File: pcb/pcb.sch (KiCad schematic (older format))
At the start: 9 parts, among them J1 Conn_01x02, J2 Conn_01x04_Male, U1 MCP73811T-420I-OT, U2 LD39050PU33R, U3 ESP8266-12E_ESP-12E

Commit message: finish the shcematic design
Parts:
- removed D1: D_Schottky, Diode_SMD:D_SMA_Handsoldering, symbol Device:D_Schottky
- removed J2: Conn_01x04_Male, Connector_PinSocket_2.54mm:PinSocket_1x04_P2.54mm_Vertical, symbol Connector:Conn_01x04_Male
- removed RN?: R_Pack04, symbol Device:R_Pack04
- removed U1: MCP73811T-420I-OT, Package_TO_SOT_SMD:SOT-23-5, symbol Battery_Management:MCP73811T-420I-OT
- removed U2: LD39050PU33R, SON95P300X300X100-7N, symbol LD39050PU33R:LD39050PU33R
- removed U3: ESP8266-12E_ESP-12E, XCVR_ESP8266-12E/ESP-12E, symbol ESP8266-12E_ESP-12E:ESP8266-12E_ESP-12E
- added C3: 10u, Capacitor_SMD:C_0603_1608Metric_Pad1.05x0.95mm_HandSolder, symbol Device:C
- added C4: 100nF, Capacitor_SMD:C_0603_1608Metric, symbol Device:C
- added C5, C6, C7: 100n, Capacitor_SMD:C_0603_1608Metric, symbol Device:C
- added D1: SP0503BAHTG, digikey-footprints:SOT-143-4, symbol dk_TVS-Diodes:SP0503BAHTG
- added H1, H2, H3: MountingHole_Pad, MountingHole:MountingHole_3.2mm_M3_DIN965_Pad, symbol Mechanical:MountingHole_Pad
- added H4: MountingHole_Pad, MountingHole:MountingHole_3.2mm_M3, symbol Mechanical:MountingHole_Pad
- added J2: USB_B_Micro, Connector_USB:USB_Micro-B_Molex-105017-0001, symbol Connector:USB_B_Micro
- added Q1: Si2371EDS, Package_TO_SOT_SMD:SOT-23, symbol Transistor_FET:Si2371EDS
- added Q2, Q3: MMBT2222A-TP, digikey-footprints:SOT-23-3, symbol dk_Transistors-Bipolar-BJT-Single:MMBT2222A-TP
- added R1: 2k, Resistor_SMD:R_0603_1608Metric_Pad1.05x0.95mm_HandSolder, symbol Device:R_US
- added R10, R11, R12, R9: 10k, Resistor_SMD:R_0603_1608Metric, symbol Device:R_US
- added R2, R3: 10k, Resistor_SMD:R_0603_1608Metric_Pad1.05x0.95mm_HandSolder, symbol Device:R_US
- added R4: R_Pack04_Split, Resistor_SMD:R_Array_Concave_4x0603, symbol Device:R_Pack04_Split
- added R5, R6: 100k, Resistor_SMD:R_0603_1608Metric_Pad1.05x0.95mm_HandSolder, symbol Device:R_US
- added R7, R8: 10k, Resistor_SMD:R_Array_Concave_4x0603, symbol Device:R_Pack04_Split
- added U1: LD1117S33CTR, digikey-footprints:SOT-223, symbol dk_PMIC-Voltage-Regulators-Linear:LD1117S33CTR
- added U2: MCP73831-2-OT, Package_TO_SOT_SMD:SOT-23-5, symbol Battery_Management:MCP73831-2-OT
- added U3: CP2104, Package_DFN_QFN:QFN-24-1EP_4x4mm_P0.5mm_EP2.6x2.6mm, symbol Interface_USB:CP2104
- added U4: CCS811, Package_LGA:AMS_LGA-10-1EP_2.7x4mm_P0.6mm, symbol Sensor_Gas:CCS811
- added U5: ESP-12F, RF_Module:ESP-12E, symbol RF_Module:ESP-12F
- added U6: BME280, digikey-footprints:Pressure_Sensor_LGA-8_2.5x2.5mm_BME280, symbol dk_Humidity-Moisture-Sensors:BME280
- added U7: TSL2561, Kevin_Lutzer:TSL2561, symbol Kevin_Lutzer:TSL2561
- C1: value 1uf -> 1u
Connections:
- net labels added: BAT_LVL, CCS_nINT, I2C_SCK, I2C_SDA, UART_RX, UART_TX, nBAT_STAT, nBOOT, nINT, nRST
- net labels removed: BOOT, EN, RST, RX, TX
- wire segments 47 -> 163
- no-connect marks 0 -> 26
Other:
- note added: "1K - 1A\n2K - 500mA\n10K - 100mA\n"
- note added: "Lipo Charger and Regulator"
- note added: "Sensor Array"
- note added: "The CP210x series of chips requires a driver. There is also a built in Boot/Rst trigger using the DTR and RTS controls.\nhttps://www.silabs.com/products/development-tools/software/usb-to-uart-bridge-vcp-drivers"
- note added: "USB Bridge"
- moved on the sheet: C1, C2

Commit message: get the update done on the pcb design, finish it
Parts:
- removed R10, R11, R12, R9: 10k, Resistor_SMD:R_0603_1608Metric, symbol Device:R_US
- removed R2, R3: 10k, Resistor_SMD:R_0603_1608Metric_Pad1.05x0.95mm_HandSolder, symbol Device:R_US
- removed unit 4 of R4
- removed unit 3 of R4
- removed U1: LD1117S33CTR, digikey-footprints:SOT-223, symbol dk_PMIC-Voltage-Regulators-Linear:LD1117S33CTR
- added D2: MBR120ESFT1G, Diode_SMD:D_SOD-123, symbol Kevin_Lutzer:MBR120ESFT1G
- added R2: 10k, Resistor_SMD:R_Array_Convex_4x0603, symbol Device:R_Pack04_Split
- added R9: 10k, Resistor_SMD:R_Array_Convex_4x1206, symbol Device:R_Pack04_Split
- added SW1: PCM12, Button_Switch_SMD:SW_SPDT_PCM12, symbol Switch:SW_SPDT
- added U1: LD56100, Package_DFN_QFN:DFN-8-1EP_2x2mm_P0.45mm_EP0.64x1.38mm, symbol Kevin_Lutzer:LD56100
- H1, H2, H3: footprint MountingHole:MountingHole_3.2mm_M3_DIN965_Pad -> MountingHole:MountingHole_2.2mm_M2_DIN965_Pad
- H4: footprint MountingHole:MountingHole_3.2mm_M3 -> MountingHole:MountingHole_2.2mm_M2
- R4: value R_Pack04_Split -> 10k
- R7: footprint Resistor_SMD:R_Array_Concave_4x0603 -> Resistor_SMD:R_Array_Convex_4x1206
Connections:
- net labels added: CCS_nWAKE
- wire segments 163 -> 184
- no-connect marks 26 -> 25
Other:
- moved on the sheet: C1, C2, H1, H2, H3, H4, R5, R6, R7A, R7B, R8A, R8B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

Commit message: try update the node modules
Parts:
- removed C1: 1u, Capacitor_SMD:C_0603_1608Metric_Pad1.05x0.95mm_HandSolder, symbol Device:C
- removed C5, C6, C7: 100n, Capacitor_SMD:C_0603_1608Metric, symbol Device:C
- removed D1: SP0503BAHTG, digikey-footprints:SOT-143-4, symbol dk_TVS-Diodes:SP0503BAHTG
- removed D2: MBR120ESFT1G, Diode_SMD:D_SOD-123, symbol Kevin_Lutzer:MBR120ESFT1G
- removed H2, H3: MountingHole_Pad, MountingHole:MountingHole_2.2mm_M2_DIN965_Pad, symbol Mechanical:MountingHole_Pad
- removed J1: Conn_01x02, Connector_JST:JST_XH_S2B-XH-A-1_1x02_P2.50mm_Horizontal, symbol Connector_Generic:Conn_01x02
- removed J2: USB_B_Micro, Connector_USB:USB_Micro-B_Molex-105017-0001, symbol Connector:USB_B_Micro
- removed Q1: Si2371EDS, Package_TO_SOT_SMD:SOT-23, symbol Transistor_FET:Si2371EDS
- removed Q2, Q3: MMBT2222A-TP, digikey-footprints:SOT-23-3, symbol dk_Transistors-Bipolar-BJT-Single:MMBT2222A-TP
- removed R1: 2k, Resistor_SMD:R_0603_1608Metric_Pad1.05x0.95mm_HandSolder, symbol Device:R_US
- removed R2: 10k, Resistor_SMD:R_Array_Convex_4x0603, symbol Device:R_Pack04_Split
- removed R4, R8: 10k, Resistor_SMD:R_Array_Concave_4x0603, symbol Device:R_Pack04_Split
- removed R5, R6: 100k, Resistor_SMD:R_0603_1608Metric_Pad1.05x0.95mm_HandSolder, symbol Device:R_US
- removed R7, R9: 10k, Resistor_SMD:R_Array_Convex_4x1206, symbol Device:R_Pack04_Split
- removed U2: MCP73831-2-OT, Package_TO_SOT_SMD:SOT-23-5, symbol Battery_Management:MCP73831-2-OT
- removed U4: CCS811, Package_LGA:AMS_LGA-10-1EP_2.7x4mm_P0.6mm, symbol Sensor_Gas:CCS811
- removed U7: TSL2561, Kevin_Lutzer:TSL2561, symbol Kevin_Lutzer:TSL2561
- added C10: 1u, Capacitor_SMD:C_0603_1608Metric, symbol Device:C
- added C8: 10u, Capacitor_SMD:C_0603_1608Metric, symbol Device:C
- added C9, C? (x3): 100n, Capacitor_SMD:C_0603_1608Metric, symbol Device:C
- added D1: WS2812B, LED_SMD:LED_WS2812B_PLCC4_5.0x5.0mm_P3.2mm, symbol LED:WS2812B
- added H? (x2): MountingHole_Pad, MountingHole:MountingHole_2.2mm_M2_ISO14580_Pad, symbol Mechanical:MountingHole_Pad
- added J1: USB_B_Mini, Connector_USB:USB_Micro-B_Molex-105017-0001, symbol Connector:USB_B_Mini
- added Q1, Q2: BSS138DW-7-F, digikey-footprints:SOT-363, symbol dk_Transistors-FETs-MOSFETs-Arrays:BSS138DW-7-F
- added R2, R3, R4: 10k, Resistor_SMD:R_0603_1608Metric, symbol Device:R_US
- added R5, RN1: 10k, Resistor_SMD:R_Array_Convex_4x0603, symbol Device:R_Pack04_Split
- added SW2, SW3: PTS645Vx83, Button_Switch_THT:SW_Tactile_SPST_Angled_PTS645Vx58-2LFS, symbol Switch:SW_SPST
- added U2: MIC5225-1.8YM5, Package_TO_SOT_SMD:SOT-23-5, symbol Regulator_Linear:MIC5504-1.8YM5
- added U4: TSL2591, Kevin_Lutzer:TSL2591, symbol Kevin_Lutzer:TSL2591
- added U7: SGP30, Kevin_Lutzer:SGP30, symbol Kevin_Lutzer:SGP30
- added U?: LD1117S33CTR, digikey-footprints:SOT-223, symbol dk_PMIC-Voltage-Regulators-Linear:LD1117S33CTR
- C2: footprint Capacitor_SMD:C_0603_1608Metric_Pad1.05x0.95mm_HandSolder -> Capacitor_SMD:C_0805_2012Metric
- C3: value 10u -> 100n; footprint Capacitor_SMD:C_0603_1608Metric_Pad1.05x0.95mm_HandSolder -> Capacitor_SMD:C_0603_1608Metric
- C4: value 100nF -> 1u
- H1: footprint MountingHole:MountingHole_2.2mm_M2_DIN965_Pad -> MountingHole:MountingHole_2.2mm_M2
- SW1: value PCM12 -> OS102011MA1QN1‎; footprint Button_Switch_SMD:SW_SPDT_PCM12 -> Button_Switch_THT:SW_CuK_OS102011MA1QN1_SPDT_Angled
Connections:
- net labels added: +1V8, MODE, RGB_LED, UART_DTR, UART_RTS
- net labels removed: +BATT, BAT_LVL, CCS_nINT, CCS_nWAKE, nBAT_STAT
- wire segments 184 -> 180
- no-connect marks 25 -> 28
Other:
- note added: "Regulators (3.3V and 1.8V)"
- note added: "The 3.3V Regulator is rated at 1A, It is to supply power to the ESP and most\nof the sensors. The 1.8V Regular is rated at 150mA and is for the CP60 gas\nsensor."
- note added: "Trigger circuit for the boot/rst \nesp8266 sequence needed for \nprogramming"
- note removed: "1K - 1A\n2K - 500mA\n10K - 100mA\n"
- note removed: "Lipo Charger and Regulator"
- moved on the sheet: C2, C4, H4, U6

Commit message: update the pcb stuff
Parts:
- removed Q2: BSS138DW-7-F, digikey-footprints:SOT-363, symbol dk_Transistors-FETs-MOSFETs-Arrays:BSS138DW-7-F
- removed RN1: 10k, Resistor_SMD:R_Array_Convex_4x0603, symbol Device:R_Pack04_Split
- removed SW1: OS102011MA1QN1‎, Button_Switch_THT:SW_CuK_OS102011MA1QN1_SPDT_Angled, symbol Switch:SW_SPDT
- removed U1: LD56100, Package_DFN_QFN:DFN-8-1EP_2x2mm_P0.45mm_EP0.64x1.38mm, symbol Kevin_Lutzer:LD56100
- removed U4: TSL2591, Kevin_Lutzer:TSL2591, symbol Kevin_Lutzer:TSL2591
- removed U6: BME280, digikey-footprints:Pressure_Sensor_LGA-8_2.5x2.5mm_BME280, symbol dk_Humidity-Moisture-Sensors:BME280
- removed U7: SGP30, Kevin_Lutzer:SGP30, symbol Kevin_Lutzer:SGP30
- removed U?: LD1117S33CTR, digikey-footprints:SOT-223, symbol dk_PMIC-Voltage-Regulators-Linear:LD1117S33CTR
- added D2: SP0503BAHT, Package_TO_SOT_SMD:SOT-143, symbol Power_Protection:SP0503BAHT
- added SW1: PTS645Vx83, Button_Switch_THT:SW_Tactile_SPST_Angled_PTS645Vx58-2LFS, symbol Switch:SW_SPST
- added U1: AP2112K-3.3, Package_TO_SOT_SMD:SOT-23-5, symbol Regulator_Linear:AP2112K-3.3
- C2: value 10u -> 47u
- C4: value 1u -> 100n
- C8: footprint Capacitor_SMD:C_0603_1608Metric -> Capacitor_SMD:C_0805_2012Metric
- Q1: symbol dk_Transistors-FETs-MOSFETs-Arrays:BSS138DW-7-F -> pcb-rescue:BSS138DW-7-F-dk_Transistors-FETs-MOSFETs-Arrays
- gave numbers to parts that had none: 5
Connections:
- net labels removed: UART_DTR, UART_RTS
- wire segments 180 -> 140
- no-connect marks 28 -> 26
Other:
- note added: "I/O - Buttons and LEDs"
- note added: "USB/UART Bridge + Auto Reset"
- note removed: "Sensor Array"
- note removed: "USB Bridge"
- moved on the sheet: C1, C10, C2, C3, C5, C6, C8, C9, D1, H1, H2, H3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

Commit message: finish laying out most of the pcb parts
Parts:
- removed C3: 100n, Capacitor_SMD:C_0603_1608Metric, symbol Device:C
- removed Q1: BSS138DW-7-F, digikey-footprints:SOT-363, symbol pcb-rescue:BSS138DW-7-F-dk_Transistors-FETs-MOSFETs-Arrays
- removed R5: 10k, Resistor_SMD:R_Array_Convex_4x0603, symbol Device:R_Pack04_Split
- added C7: 10u, Capacitor_SMD:C_0805_2012Metric, symbol Device:C
- added D3, D4: LED, LED_SMD:LED_0603_1608Metric, symbol Device:LED
- added Q1: BSS138DW-7-F, digikey-footprints:SOT-363, symbol dk_Transistors-FETs-MOSFETs-Arrays:BSS138DW-7-F
- added R1, R6: 470, Resistor_SMD:R_0603_1608Metric, symbol Device:R_Small_US
- added R5, R7, R8, R9: 10k, Resistor_SMD:R_0603_1608Metric, symbol Device:R_Small_US
- C10: value 1u -> 10u
- C9: value 100n -> 10u
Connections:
- net +3V3: now also C1.1, D3.1 (K), D4.1 (K), R5.1, R7.1, R8.1; no longer C9.1, U2.1 (VIN), U2.3 (EN)
- net +5V: now also C9.1, D2.2 (K), U2.1 (VIN), U2.3 (EN), C7.1; no longer D2.4 (K)
- net GND: now also C7.2, R9.2
- net MODE: now also SW1.2 (B), U5.7 (GPIO13); no longer SW3.2 (B), U5.14 (SCLK)
- net nBOOT: now also SW2.2 (B), Q1.3 (D1), R8.2; no longer SW1.2 (B)
- net nRST: now also SW3.2 (B), Q1.6 (D2), R5.2; no longer C1.1, SW2.2 (B)
- net at U3.13 (GPIO.1): now also R1.2
- net at U3.14 (GPIO.0): now also R6.2
- net at R4.2, U3.19 (RTS): now also Q1.1 (S2)
- net at R3.2, U3.23 (DTR): now also Q1.4 (S1)
- net at J1.3 (D+), U3.3 (D+): no longer D2.2 (K)
- net at J1.2 (D-), U3.4 (D-): no longer D2.3 (K)
- net at R3.1: now also Q1.2 (G2)
- net at R4.1: now also Q1.5 (G1)
- net at U5.16 (GPIO15): now also R9.1
- net at U5.3 (EN): now also R7.2
- new net: D4.2 (A), R6.1
- new net: D3.2 (A), R1.1
- no-connect marks 26 -> 25
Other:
- moved on the sheet: D2, SW1, SW2, SW3

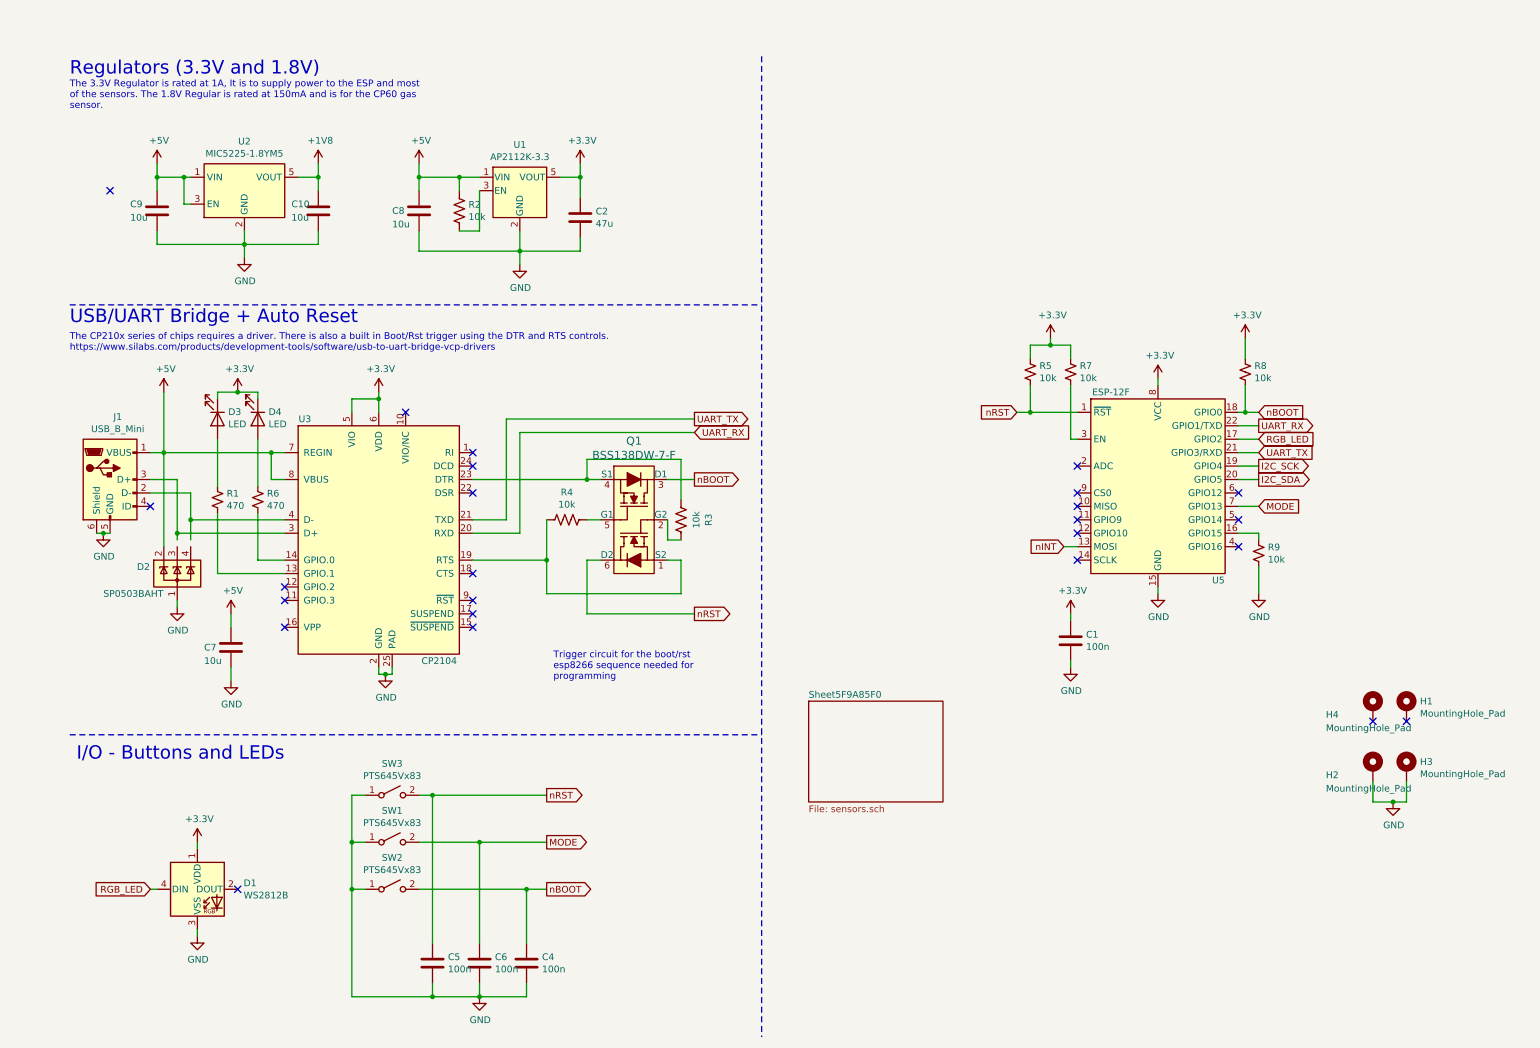
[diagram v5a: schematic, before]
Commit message: finish the routing of the pcb all that is left is to clean up the silkscreen
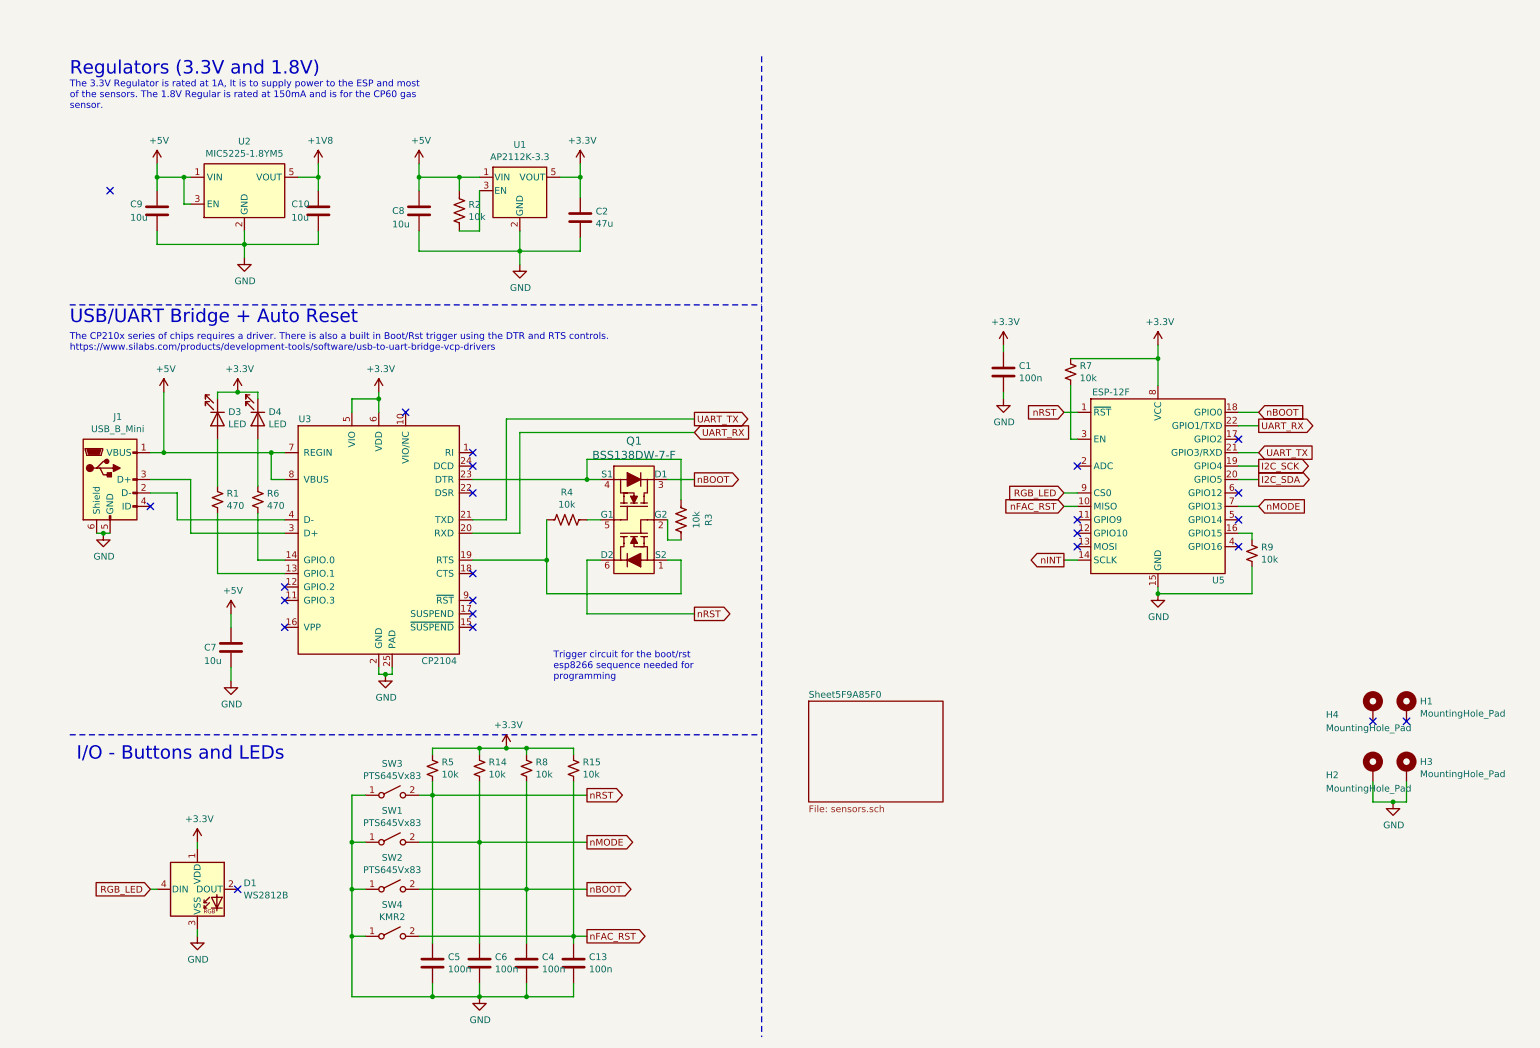
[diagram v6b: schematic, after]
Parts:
- removed D2: SP0503BAHT, Package_TO_SOT_SMD:SOT-143, symbol Power_Protection:SP0503BAHT
- added C13: 100n, Capacitor_SMD:C_0603_1608Metric, symbol Device:C
- added R14, R15: 10k, Resistor_SMD:R_0603_1608Metric, symbol Device:R_Small_US
- added SW4: KMR2, Button_Switch_SMD:SW_Push_1P1T_NO_CK_KMR2, symbol Switch:SW_SPST
- C7, C8: footprint Capacitor_SMD:C_0805_2012Metric -> Capacitor_SMD:C_0603_1608Metric
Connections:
- net +3V3: now also R14.1, R15.1
- net GND: now also C13.2, SW4.1 (A)
- net RGB_LED: now also U5.9 (CS0); no longer U5.17 (GPIO2)
- net nINT: now also U5.14 (SCLK); no longer U5.13 (MOSI)
- net nFAC_RST: now reaches U5.10 (MISO)
- net nFAC_RST: now also C13.1, R15.2, SW4.2 (B)
- net MODE renamed nMODE
- net nMODE: now also R14.2
- no-connect marks 25 -> 24
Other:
- moved on the sheet: C1, R5, R8, R9

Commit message: add gerbers for room monitor v1
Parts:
- added J4: UART_BUS, Connector_PinHeader_2.54mm:PinHeader_1x02_P2.54mm_Vertical, symbol Connector:Conn_01x02_Male
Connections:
- net +3V3: now also D3.2 (A), D4.2 (A); no longer D3.1 (K), D4.1 (K)
- net UART_RX: now also J4.1 (Pin_1)
- net UART_TX: now also J4.2 (Pin_2)
- net at R6.1: now also D4.1 (K); no longer D4.2 (A)
- net at R1.1: now also D3.1 (K); no longer D3.2 (A)
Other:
- note added: "ESP-12F w/ Sensor Subblock"
- note added: "Mounting Holes"
- moved on the sheet: C1, C13, C4, C5, C6, D3, D4, H1, H2, H3, H4, R14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

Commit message: WIP
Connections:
- net RGB_LED: now also U5.6 (GPIO12); no longer U5.9 (CS0)
- net nFAC_RST: now also U5.5 (GPIO14); no longer U5.10 (MISO)
- net nINT: now also U5.17 (GPIO2); no longer U5.14 (SCLK)
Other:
- moved on the sheet: R9
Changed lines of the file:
@@
 	6450 1700 6500 1700
 Wire Wire Line
-	7700 2400 7800 2400
+	7700 2400 7750 2400
 Text GLabel 7850 1900 2    50   Output ~ 0
 I2C_SCK
@@
 NoConn ~ 6500 2300
 NoConn ~ 6500 2400
-NoConn ~ 7700 2500
-NoConn ~ 7700 2300
-NoConn ~ 7700 2100
 Wire Notes Line
 	5650 500  5650 7800
-Text GLabel 6400 2100 0    50   Input ~ 0
-RGB_LED
 $Comp
 L Device:R_US R2
@@
 NoConn ~ 1750 6700
 NoConn ~ 3000 3150
-Text GLabel 6400 2600 0    50   Output ~ 0
+Text GLabel 7850 1700 2    50   Output ~ 0
 nINT
-Wire Wire Line
-	6400 2600 6500 2600
 $Comp
 L dk_Transistors-FETs-MOSFETs-Arrays:BSS138DW-7-F Q1
@@
 L Device:R_Small_US R9
 U 1 1 5F341E1A
-P 7800 2550
-F 0 "R9" H 7868 2596 50  0000 L CNN
-F 1 "10k" H 7868 2505 50  0000 L CNN
-F 2 "Resistor_SMD:R_0603_1608Metric" H 7800 2550 50  0001 C CNN
-F 3 "~" H 7800 2550 50  0001 C CNN
-	1    7800 2550
-	1    0    0    -1
-$EndComp
-Wire Wire Line
-	7800 2400 7800 2450
+P 7750 2700
+F 0 "R9" H 7818 2746 50  0000 L CNN
+F 1 "10k" H 7818 2655 50  0000 L CNN
+F 2 "Resistor_SMD:R_0603_1608Metric" H 7750 2700 50  0001 C CNN
+F 3 "~" H 7750 2700 50  0001 C CNN
+	1    7750 2700
+	1    0    0    -1
+$EndComp
+Wire Wire Line
+	7750 2400 7750 2600
 Wire Wire Line
 	6450 1300 6450 1700
@@
 	7100 1100 7100 1000
 Wire Wire Line
-	7100 2850 7800 2850
+	7100 2850 7750 2850
 Connection ~ 7100 2850
 Wire Wire Line
-	7800 2650 7800 2850
-Wire Wire Line
-	6400 2100 6500 2100
+	7750 2800 7750 2850
 NoConn ~ 6500 2500
-Text GLabel 6400 2200 0    50   Input ~ 0
+Text GLabel 7850 2300 2    50   Input ~ 0
 nFAC_RST
 Wire Wire Line
-	6400 2200 6500 2200
-NoConn ~ 7700 1700
+	7850 2300 7700 2300
 Text Notes 5700 650  0    100  ~ 0
 ESP-12F w/ Sensor Subblock
@@
 Wire Wire Line
 	3500 3650 4350 3650
+Text GLabel 7850 2100 2    50   Input ~ 0
+RGB_LED
+Wire Wire Line
+	7700 2100 7850 2100
+Wire Wire Line
+	7700 1700 7850 1700
+NoConn ~ 7700 2500
+NoConn ~ 6500 2100
+NoConn ~ 6500 2200
+NoConn ~ 6500 2600
 $EndSCHEMATC
